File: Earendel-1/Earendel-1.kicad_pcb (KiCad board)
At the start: 2 copper layers, 34 parts, among them J1 SAMTEC-CES-110-01-X-D, J4 85_SMA-50-0-144_111_YH, U1 ATA8510-GHQW, U2 STM32F411CCUx, Y1 XRCGB24M000F0G00R0

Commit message: first Routing
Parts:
- removed J1: SAMTEC-CES-110-01-X-D, Connector_Coaxial:SMA_Samtec_SMA-J-P-H-ST-EM1_EdgeMount
- added J2: TSW-101-05-T-T, TSW-101-05-T-T:SAMTEC_TSW-101-05-T-T, F.Cu at (63.4, 146.6)
- added J5: TSS-110-01-G-D, TSS-110-01-G-D:SAMTEC_TSS-110-01-G-D, F.Cu at (37.0, 126.7)
- added J6: TSS-110-01-G-D, TSS-110-01-G-D:SAMTEC_TSS-110-01-G-D, F.Cu at (58.8, 63.5)
- moved U1 302.8 mm to (77.5, 99.0), turned to 90 degrees
- moved U2 288.7 mm to (62.3, 100.3), turned to 180 degrees
- moved J4 276.2 mm to (84.0, 144.0)
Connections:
- U2 pad 22: unconnected-(U2-VCAP1-Pad22) -> /VCAP
- U2 pad 33: unconnected-(U2-PA12-Pad33) -> /LORA_CS
- U2 pad 42: unconnected-(U2-PB6-Pad42) -> /SCL
- U2 pad 43: unconnected-(U2-PB7-Pad43) -> /SDA
- U2 pad 8: unconnected-(U2-VSSA-Pad8) -> GND
- U2 pad 9: unconnected-(U2-VDDA-Pad9) -> /VDD

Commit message: Programmer and ATA mostly routed
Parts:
- added C15: 4.7uF, Capacitor_SMD:C_0504_1310Metric_Pad0.83x1.28mm_HandSolder, F.Cu at (54.0, 95.5)
- added J1: MTMM-101-15-G-D-105, MTMM-101-15-G-D-105:SAMTEC_MTMM-101-15-G-D-105, F.Cu at (51.0, 146.5)
- added Y2: CAA-4.000-18-3050-X, CAA-4.000-18-3050-X-R(1):XTAL_CAA-4.000-18-3050-X-R, F.Cu at (72.0, 101.5)
- moved C11 323.4 mm to (52.5, 87.5), turned to 180 degrees
- moved C12 323.2 mm to (52.5, 91.0), turned to 180 degrees
- moved Y1 298.5 mm to (56.0, 89.2), turned to -45 degrees
- moved C13 296.3 mm to (79.0, 100.5)
- moved C14 296.3 mm to (79.0, 103.5)
- moved D1 291.1 mm to (50.0, 119.7), turned to -90 degrees
- moved TP1 283.5 mm to (69.5, 92.0)
- moved TP2 228.1 mm to (132.5, 99.4)
- moved TP3 228.1 mm to (132.5, 103.2)
- moved TP4 228.1 mm to (132.5, 107.1)
- moved TP5 228.1 mm to (132.5, 110.9)
- moved TP6 228.1 mm to (136.9, 99.4)
- moved TP7 228.1 mm to (136.9, 103.2)
- moved TP8 228.1 mm to (136.9, 107.1)
- moved C1 228.1 mm to (128.5, 130.0)
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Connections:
- U2 pad 26: unconnected-(U2-PB13-Pad26) -> /SCK_2
- U2 pad 27: unconnected-(U2-PB14-Pad27) -> /MISO_2
- U2 pad 28: unconnected-(U2-PB15-Pad28) -> /MOSI_2
- U2 pad 40: /JTRST -> /NJTRST
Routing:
- net /NRST: track 0.00 -> 58.2 mm
- net /JTMS: track 0.00 -> 22.2 mm, vias 0 -> 2
- net /JTDI: track 0.00 -> 21.0 mm, vias 0 -> 1
- net /NJTRST: track 0.00 -> 20.3 mm
- net /JTCLK: track 0.00 -> 17.1 mm, vias 0 -> 2
- net /STM_XTAL_-: track 0.00 -> 16.5 mm
- net /STM_XTAL_+: track 0.00 -> 15.5 mm
- net /CLK_OUT: track 0.00 -> 14.6 mm
- net /Wake_Up: track 0.00 -> 14.6 mm, vias 0 -> 2
- net /JTDO: track 0.00 -> 12.0 mm
- net /NSS: track 0.00 -> 8.75 mm
- net /VCAP: track 0.00 -> 6.77 mm, vias 0 -> 2
- net /MISO: track 0.00 -> 6.30 mm, vias 0 -> 2
- net /XTAL+: track 0.00 -> 6.26 mm
- net /XTAL-: track 0.00 -> 6.25 mm
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
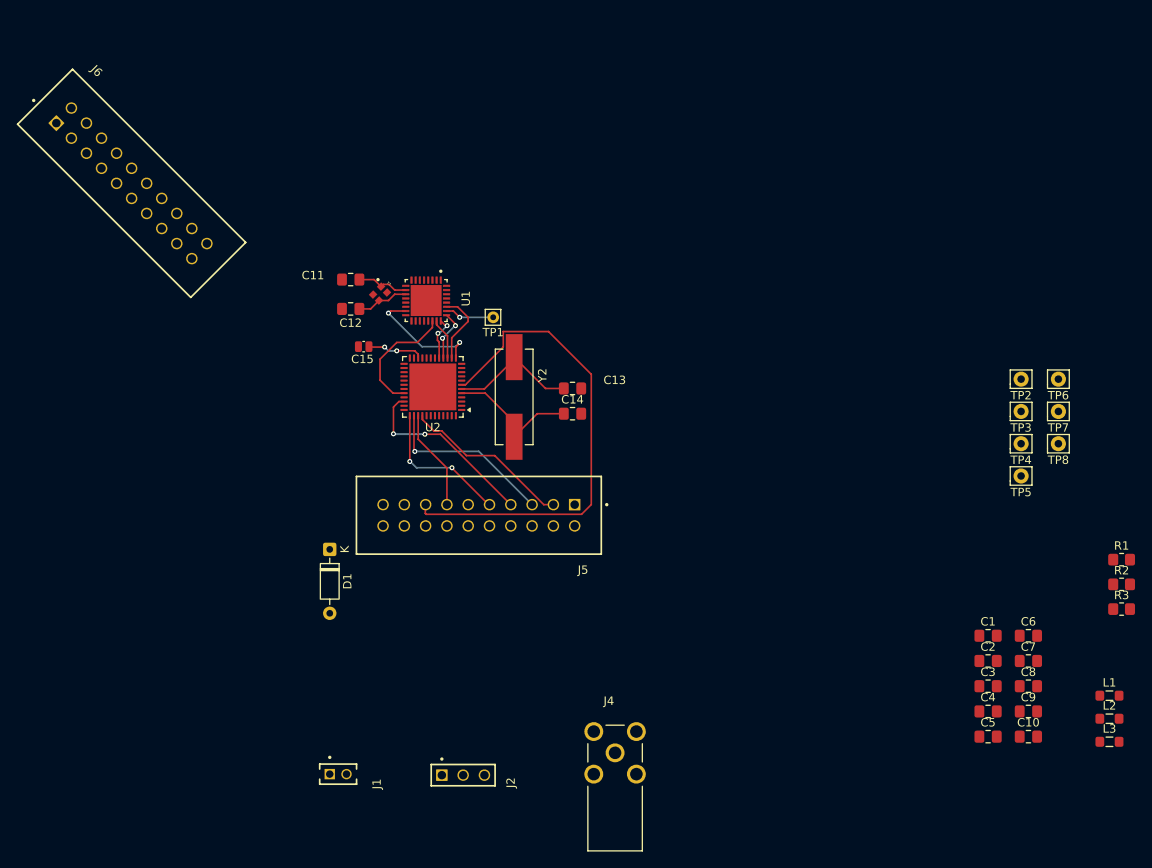
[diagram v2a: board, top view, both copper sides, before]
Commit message: Programmer and ATA mostly routed
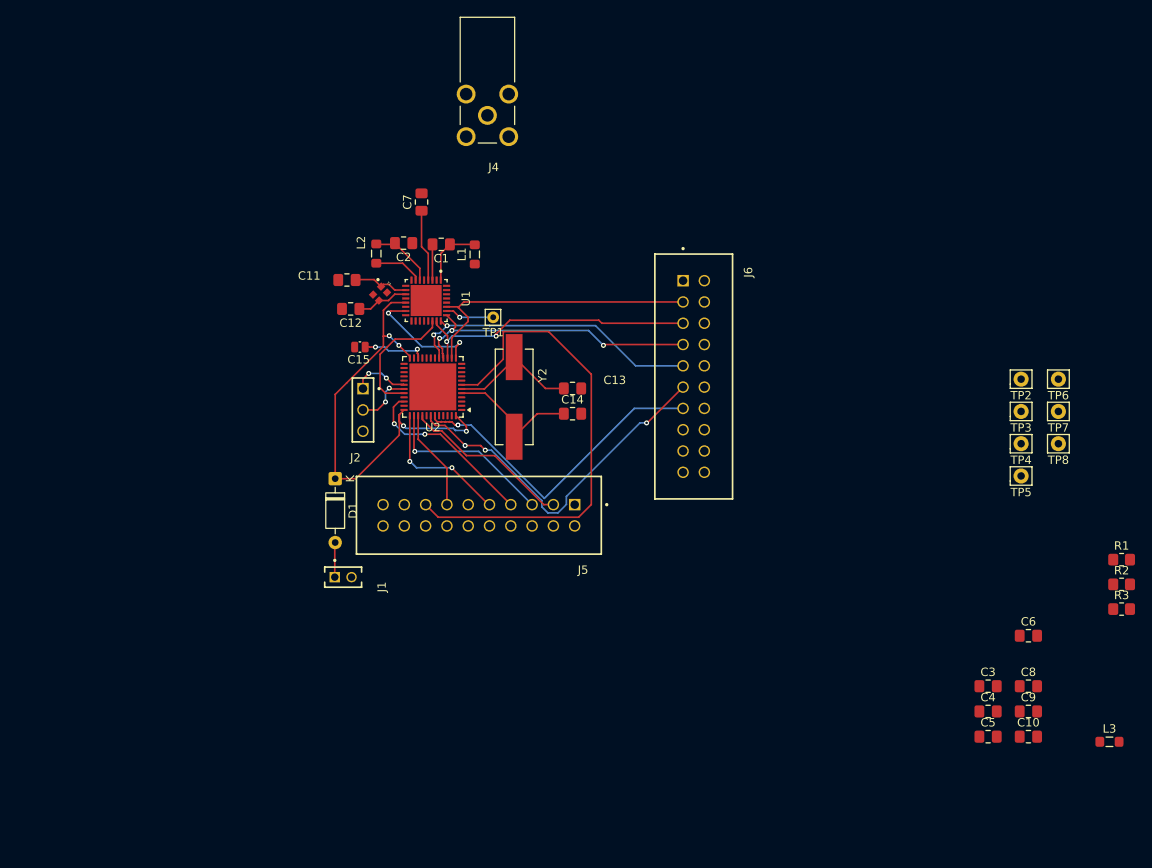
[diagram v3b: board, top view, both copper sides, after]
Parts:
- moved L2 103.6 mm to (55.5, 84.4), turned to -90 degrees
- moved L1 92.2 mm to (67.3, 84.5), turned to 90 degrees
- moved C7 90.8 mm to (61.0, 78.2), turned to 90 degrees
- moved C2 85.7 mm to (58.8, 83.2), turned to 180 degrees
- moved C1 80.2 mm to (63.3, 83.3), turned to 180 degrees
- moved J4 77.6 mm to (68.8, 67.9), turned to 180 degrees
- moved J6 77.1 mm to (92.2, 87.6), turned to -90 degrees
- moved J2 47.1 mm to (54.0, 100.5), turned to 180 degrees
- moved J1 23.5 mm to (51.6, 123.0)
- moved D1 8.46 mm to (50.6, 111.2)
- moved C11 0.45 mm to (52.0, 87.5)
- moved C15 0.45 mm to (53.6, 95.5)
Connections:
- J6 pad 01: /CLK_OUT -> unconnected-(J6-Pad01)
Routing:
- net /VDD: track 0.00 -> 54.8 mm, vias 0 -> 4
- net /SCL: track 0.00 -> 42.5 mm, vias 0 -> 3
- net /SDA: track 0.00 -> 38.5 mm, vias 0 -> 1
- net /MOSI: track 5.51 -> 36.2 mm
- net /SCK: track 4.97 -> 34.6 mm, vias 0 -> 2
- net /MISO: track 6.30 -> 35.3 mm, vias 2 -> 3
- net /NSS: track 8.75 -> 35.8 mm
- net /SPDT_ANT: track 0.00 -> 8.61 mm
- net /SPDT_TX: track 0.00 -> 7.82 mm
- net /RFIN_LB: track 0.00 -> 7.70 mm
- net /TX: track 0.00 -> 6.87 mm, vias 0 -> 2
- net /RX: track 0.00 -> 6.72 mm, vias 0 -> 2
- net /RF_OUT: track 0.00 -> 5.81 mm
- net /SPDT_RX: track 0.00 -> 4.27 mm
- net /V+: track 0.00 -> 4.15 mm
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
